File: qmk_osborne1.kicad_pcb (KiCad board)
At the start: 2 copper layers, 24.1 x 52.1 mm, 2 parts

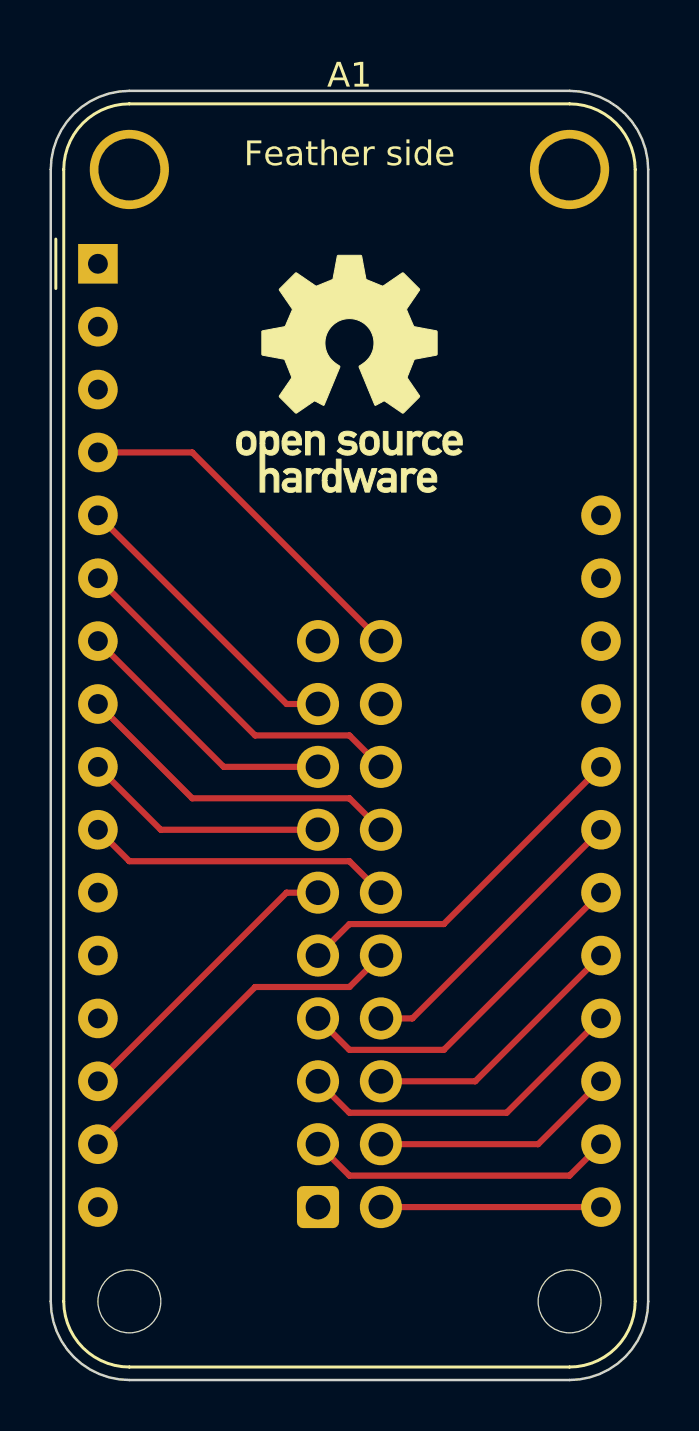
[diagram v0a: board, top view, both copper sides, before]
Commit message: Moved row pins to be able to monitor battery voltage
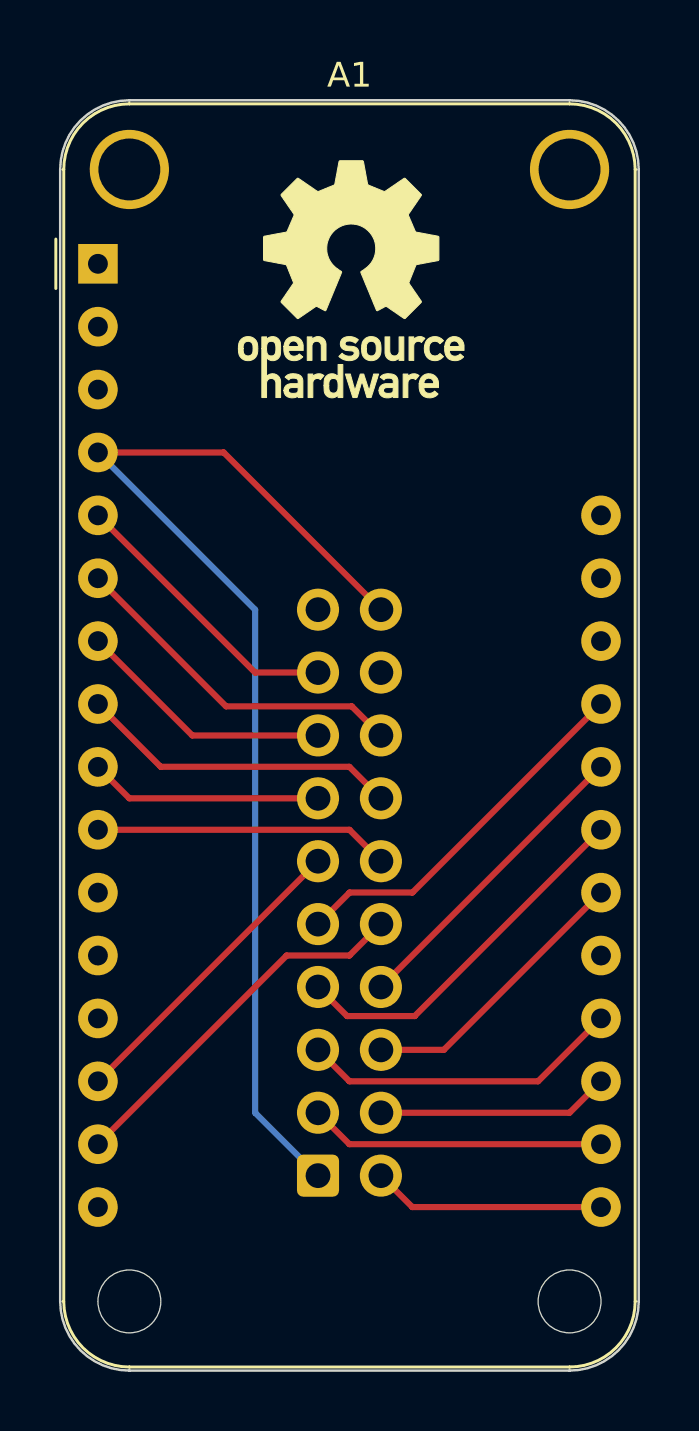
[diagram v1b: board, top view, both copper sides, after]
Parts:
- moved Keyboard1 1.27 mm to (68.6, 97.8)
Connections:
- A1 pad 10: unconnected-(A1-Pad10) -> Net-(A1-Pad10)
- A1 pad 14: unconnected-(A1-Pad14) -> Net-(A1-Pad14)
- A1 pad 15: unconnected-(A1-Pad15) -> Net-(A1-Pad15)
- A1 pad 17: unconnected-(A1-Pad17) -> Net-(A1-Pad17)
- A1 pad 18: unconnected-(A1-Pad18) -> Net-(A1-Pad18)
- A1 pad 19: unconnected-(A1-Pad19) -> Net-(A1-Pad19)
- A1 pad 20: unconnected-(A1-Pad20) -> Net-(A1-Pad20)
- A1 pad 22: unconnected-(A1-Pad22) -> Net-(A1-Pad22)
- A1 pad 23: unconnected-(A1-Pad23) -> Net-(A1-Pad23)
- A1 pad 24: unconnected-(A1-Pad24) -> Net-(A1-Pad24)
- A1 pad 25: unconnected-(A1-Pad25) -> Net-(A1-Pad25)
- A1 pad 28: unconnected-(A1-Pad28) -> +BATT
- A1 pad 4: unconnected-(A1-Pad4) -> -BATT
- A1 pad 5: unconnected-(A1-Pad5) -> Net-(A1-Pad5)
- A1 pad 6: unconnected-(A1-Pad6) -> Net-(A1-Pad6)
- A1 pad 7: unconnected-(A1-Pad7) -> Net-(A1-Pad7)
- A1 pad 8: unconnected-(A1-Pad8) -> Net-(A1-Pad8)
- A1 pad 9: unconnected-(A1-Pad9) -> Net-(A1-Pad9)
- Keyboard1 pad 1: unconnected-(Keyboard1-Pad1) -> -BATT
- Keyboard1 pad 10: unconnected-(Keyboard1-Pad10) -> Net-(A1-Pad15)
- Keyboard1 pad 11: unconnected-(Keyboard1-Pad11) -> Net-(A1-Pad14)
- Keyboard1 pad 12: unconnected-(Keyboard1-Pad12) -> Net-(A1-Pad10)
- Keyboard1 pad 13: unconnected-(Keyboard1-Pad13) -> Net-(A1-Pad9)
- Keyboard1 pad 14: unconnected-(Keyboard1-Pad14) -> Net-(A1-Pad8)
- Keyboard1 pad 15: unconnected-(Keyboard1-Pad15) -> Net-(A1-Pad7)
- Keyboard1 pad 16: unconnected-(Keyboard1-Pad16) -> Net-(A1-Pad6)
- Keyboard1 pad 17: unconnected-(Keyboard1-Pad17) -> Net-(A1-Pad5)
- Keyboard1 pad 2: unconnected-(Keyboard1-Pad2) -> Net-(A1-Pad17)
- Keyboard1 pad 20: unconnected-(Keyboard1-Pad20) -> -BATT
- Keyboard1 pad 3: unconnected-(Keyboard1-Pad3) -> Net-(A1-Pad18)
- Keyboard1 pad 4: unconnected-(Keyboard1-Pad4) -> Net-(A1-Pad19)
- Keyboard1 pad 5: unconnected-(Keyboard1-Pad5) -> Net-(A1-Pad20)
- Keyboard1 pad 6: unconnected-(Keyboard1-Pad6) -> Net-(A1-Pad22)
- Keyboard1 pad 7: unconnected-(Keyboard1-Pad7) -> Net-(A1-Pad23)
- Keyboard1 pad 8: unconnected-(Keyboard1-Pad8) -> Net-(A1-Pad24)
- Keyboard1 pad 9: unconnected-(Keyboard1-Pad9) -> Net-(A1-Pad25)
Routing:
- net -BATT: track 0.00 -> 47.0 mm
- net Net-(A1-Pad25): track 0.00 -> 15.1 mm
- net Net-(A1-Pad15): track 0.00 -> 15.1 mm
- net Net-(A1-Pad23): track 0.00 -> 15.0 mm
- net unconnected-(A1-Pad4): track 14.6 -> 0.00 mm
- net unconnected-(A1-Pad24): track 14.6 -> 0.00 mm
- net unconnected-(Keyboard1-Pad16): track 14.6 -> 0.00 mm
- net unconnected-(A1-Pad22): track 14.6 -> 0.00 mm
- net unconnected-(Keyboard1-Pad10): track 14.6 -> 0.00 mm
- net Net-(A1-Pad6): track 0.00 -> 14.1 mm
- net unconnected-(Keyboard1-Pad5): track 13.5 -> 0.00 mm
- net unconnected-(A1-Pad8): track 13.5 -> 0.00 mm
- net Net-(A1-Pad20): track 0.00 -> 13.0 mm
- net Net-(A1-Pad8): track 0.00 -> 13.0 mm
- net Net-(A1-Pad24): track 0.00 -> 12.6 mm
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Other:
- board size 24.1 x 52.1 mm -> 23.4 x 51.3 mm
- board text added: "Keyboard to Feather BlueFruit adapter"
- board text removed: "Feather side"
- board text removed: "to Feather adapter"
